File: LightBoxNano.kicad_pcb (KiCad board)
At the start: 2 copper layers, 63 parts, among them J5V1 Conn_02 DNP, SW1 Knitter-Switch DRR4010

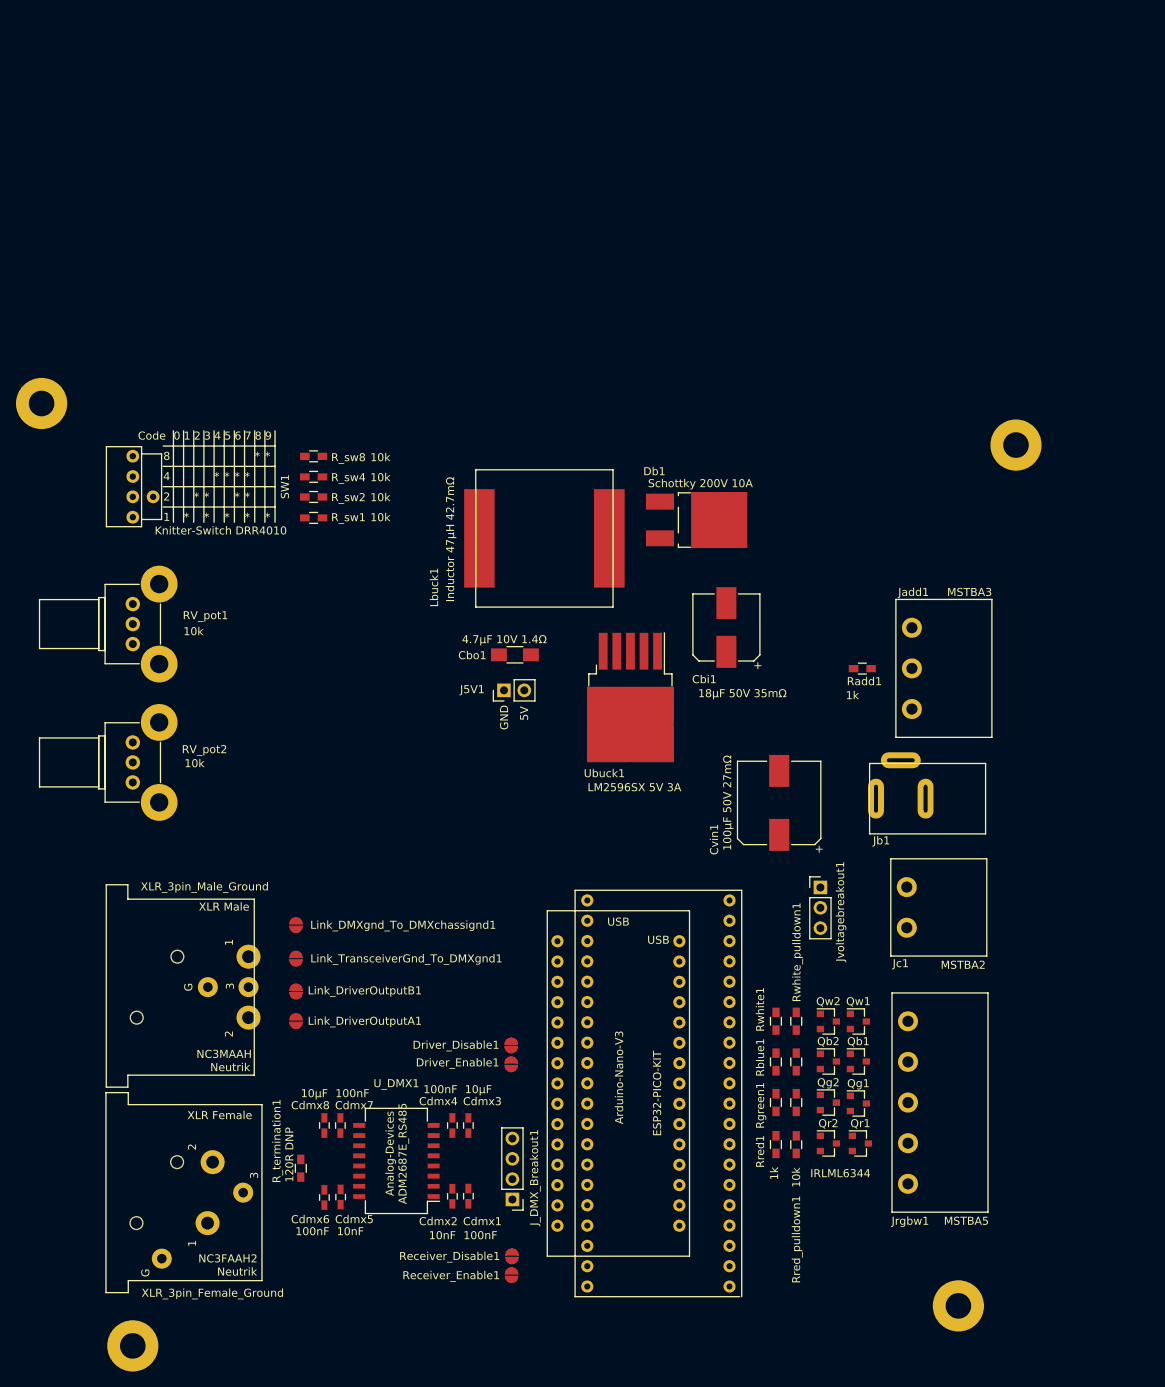
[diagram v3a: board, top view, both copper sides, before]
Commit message: Add Input Protection to PCB
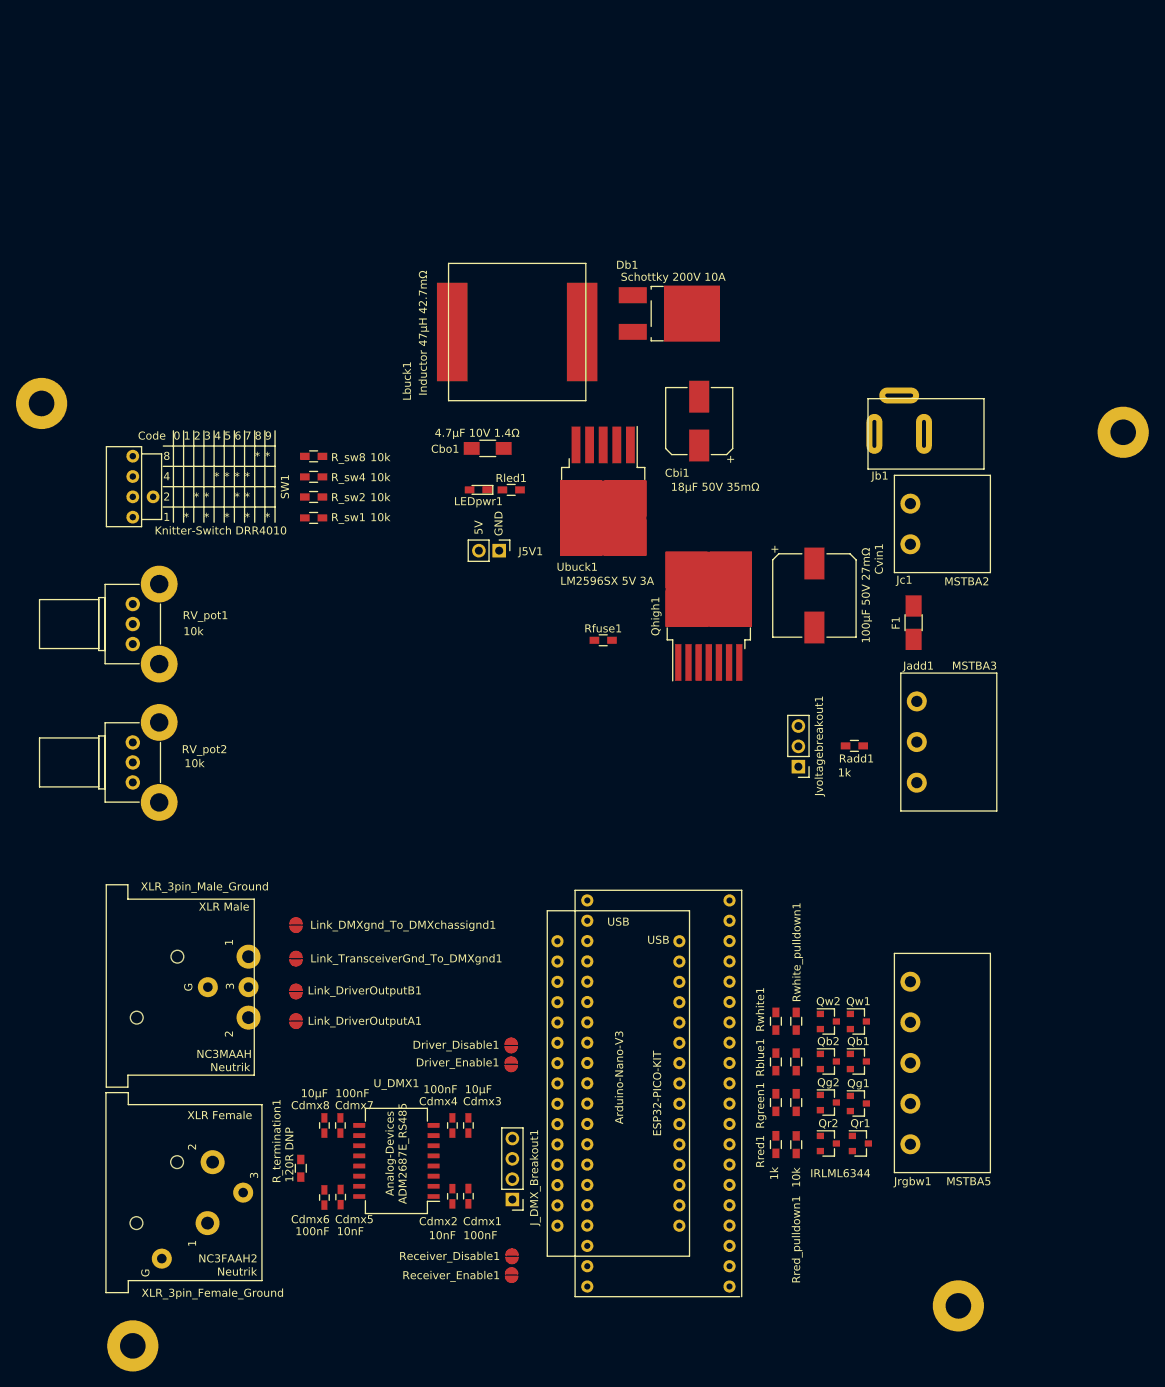
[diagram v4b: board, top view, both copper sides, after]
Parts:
- added F1: Fuse DNP, Fuse_Holders_and_Fuses:Fuse_SMD1206_HandSoldering, F.Cu at (195.0, 57.8)
- added LEDpwr1: LED Red, LEDs:LED_0603_HandSoldering, F.Cu at (140.6, 41.2)
- added Qhigh1: BTS50055-1TMC, TO_SOT_Packages_SMD:TO-263-7_TabPin4, F.Cu at (169.4, 57.0)
- added Rfuse1: 1k, Resistors_SMD:R_0603_HandSoldering, F.Cu at (156.2, 60.0)
- added Rled1: 300R, Resistors_SMD:R_0603_HandSoldering, F.Cu at (144.7, 41.2)
- moved Jc1 47.9 mm to (194.6, 48.0)
- moved Jb1 45.6 mm to (193.2, 34.2)
- moved Cvin1 26.3 mm to (182.6, 54.4), turned to 270 degrees
- moved Cbo1 26.0 mm to (141.8, 36.0)
- moved Ubuck1 26.0 mm to (156.2, 41.4)
- moved Cbi1 26.0 mm to (168.2, 32.6)
- moved Lbuck1 26.0 mm to (145.4, 21.5)
- moved Db1 26.0 mm to (164.5, 19.2)
- moved J5V1 17.5 mm to (143.2, 48.8), turned to 270 degrees
- moved Jvoltagebreakout1 15.3 mm to (180.6, 75.8), turned to 180 degrees
- moved H3 13.5 mm to (221.2, 34.0)
- moved Radd1 9.71 mm to (187.6, 73.2)
- moved Jadd1 9.23 mm to (195.4, 77.8)
- moved Jrgbw1 4.95 mm to (194.6, 123.0)
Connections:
- Cbi1 pad 1: /Vin -> /Vin_fused
- Jadd1 pad 1: /Vin -> GND
- Jadd1 pad 3: GND -> /Vin_fused
- Jrgbw1 pad 1: /Vin -> Net-(Jrgbw1-Pad1)
- Jrgbw1 pad 5: Net-(Jrgbw1-Pad5) -> /Vin_fused
- Jvoltagebreakout1 pad 3: /Vin -> /Vin_fused
- Qb1 pad 3: Net-(Jrgbw1-Pad4) -> Net-(Jrgbw1-Pad3)
- Qb2 pad 3: Net-(Jrgbw1-Pad4) -> Net-(Jrgbw1-Pad3)
- Qg1 pad 3: Net-(Jrgbw1-Pad3) -> Net-(Jrgbw1-Pad2)
- Qg2 pad 3: Net-(Jrgbw1-Pad3) -> Net-(Jrgbw1-Pad2)
- Qr1 pad 3: Net-(Jrgbw1-Pad2) -> Net-(Jrgbw1-Pad1)
- Qr2 pad 3: Net-(Jrgbw1-Pad2) -> Net-(Jrgbw1-Pad1)
- Qw1 pad 3: Net-(Jrgbw1-Pad5) -> Net-(Jrgbw1-Pad4)
- Qw2 pad 3: Net-(Jrgbw1-Pad5) -> Net-(Jrgbw1-Pad4)
- Radd1 pad 1: /Addressable -> Net-(Jadd1-Pad2)
- Radd1 pad 2: Net-(Jadd1-Pad2) -> /Addressable
- Ubuck1 pad 1: /Vin -> /Vin_fused

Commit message: Input Protection description, Pwer Switch Feedback
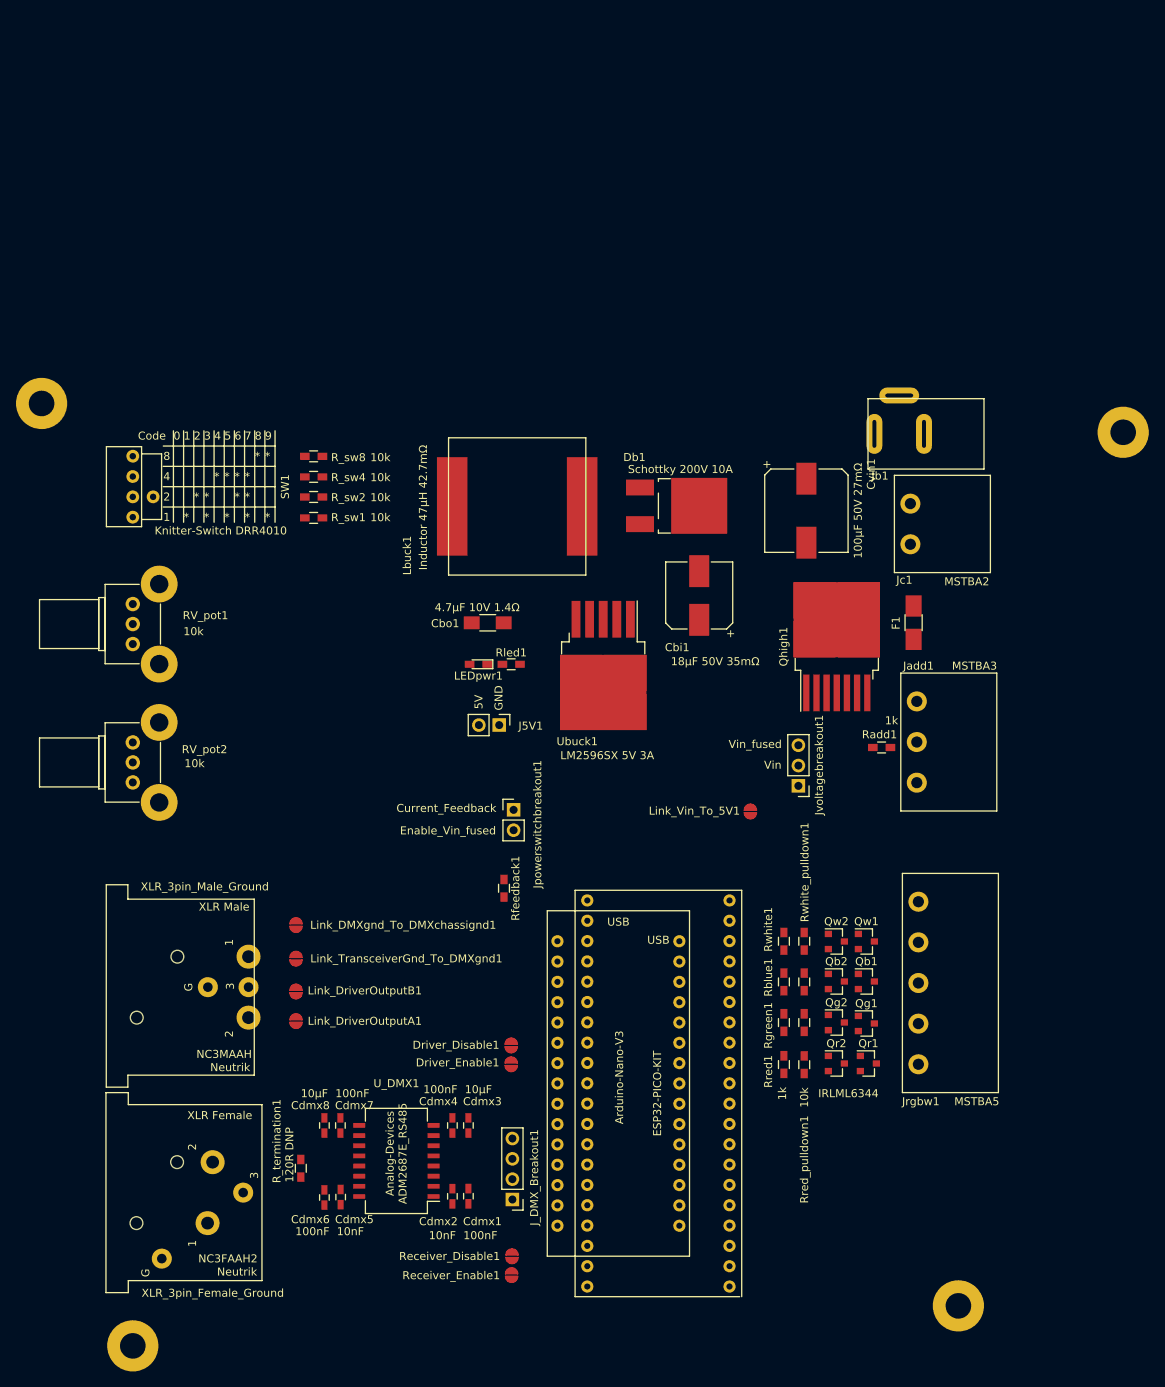
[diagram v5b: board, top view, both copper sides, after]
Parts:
- removed Rfuse1: 1k, Resistors_SMD:R_0603_HandSoldering
- added Jpowerswitchbreakout1: Conn_02 DNP, Pin_Headers:Pin_Header_Straight_1x02_Pitch2.54mm, F.Cu at (145.0, 81.2)
- added Link_Vin_To_5V1: Link Vin to 5V, ConnTest:JUMPER-SOLDER-SMD, F.Cu at (174.6, 81.4)
- added Rfeedback1: 1k, Resistors_SMD:R_0603_HandSoldering, F.Cu at (143.8, 91.0)
- moved Db1 24.0 mm to (165.4, 43.2)
- moved Cbo1 21.8 mm to (141.8, 57.8)
- moved Cbi1 21.8 mm to (168.2, 54.4)
- moved J5V1 21.8 mm to (143.2, 70.6)
- moved LEDpwr1 21.8 mm to (140.6, 63.0)
- moved Lbuck1 21.8 mm to (145.4, 43.3)
- moved Rled1 21.8 mm to (144.7, 63.0)
- moved Ubuck1 21.8 mm to (156.2, 63.1)
- moved Qhigh1 16.4 mm to (185.4, 60.8)
- moved Cvin1 10.6 mm to (181.6, 43.8)
- moved Jrgbw1 10.0 mm to (195.6, 113.0)
- moved Qb1 10.0 mm to (189.1, 102.7)
- moved Qb2 10.0 mm to (185.3, 102.7)
- moved Qg1 10.0 mm to (189.1, 107.9)
- moved Qg2 10.0 mm to (185.3, 107.8)
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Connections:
- Cbi1 pad 1: /Vin_fused -> /Vin
- MCU_esp1 pad J2_16: Net-(MCU_esp1-PadJ2_16) -> /Current_Feedback
- MCU_esp1 pad J2_17: Net-(MCU_esp1-PadJ2_17) -> /Enable_Vin_fused
- MCU_nano1 pad 16: Net-(MCU_nano1-Pad16) -> /Enable_Vin_fused
- MCU_nano1 pad 19: Net-(MCU_nano1-Pad19) -> /Current_Feedback
- Qhigh1 pad 3: GND -> /Enable_Vin_fused
- Qhigh1 pad 5: Net-(Qhigh1-Pad5) -> /Current_Feedback
- Ubuck1 pad 1: /Vin_fused -> /Vin

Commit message: Adjust PCB size to enclosure
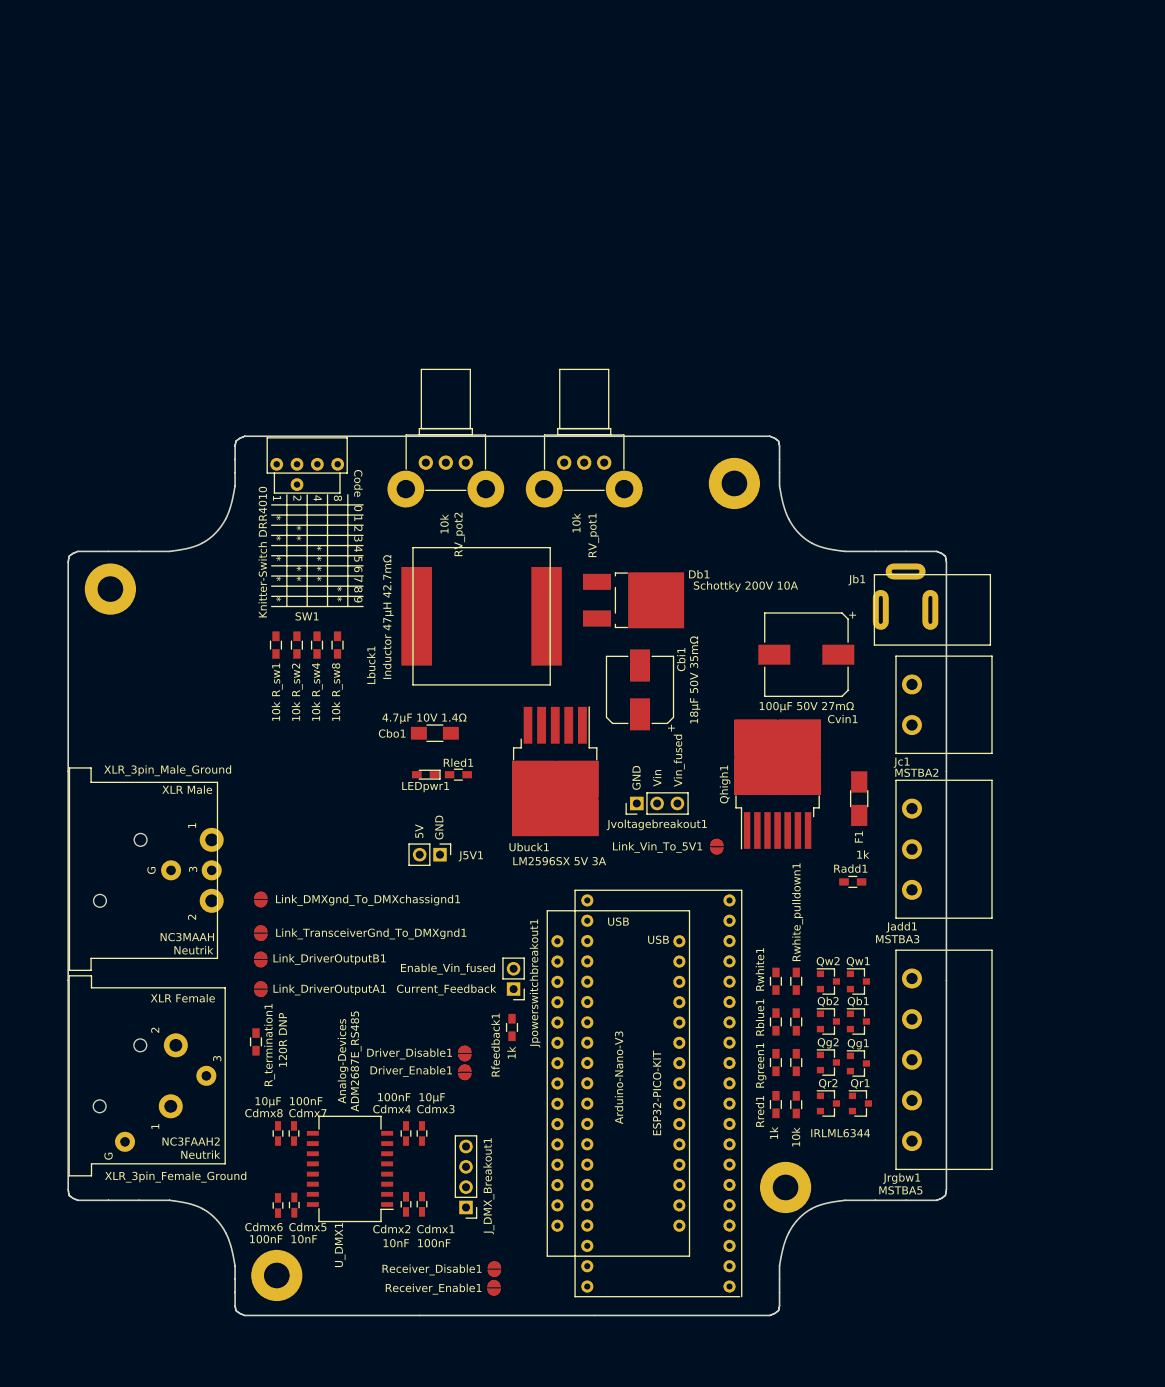
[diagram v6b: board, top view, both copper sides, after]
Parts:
- moved RV_pot1 61.5 mm to (156.3, 37.8), turned to 90 degrees
- moved RV_pot2 54.4 mm to (139.0, 37.8), turned to 90 degrees
- moved H3 49.0 mm to (172.6, 40.4)
- moved H4 26.2 mm to (179.0, 128.4)
- moved H1 24.7 mm to (94.6, 53.6)
- moved R_sw8 23.8 mm to (123.0, 60.6), turned to 90 degrees
- moved F1 23.0 mm to (188.2, 79.8)
- moved Jc1 22.6 mm to (194.8, 70.6)
- moved Jpowerswitchbreakout1 22.4 mm to (145.0, 103.6), turned to 180 degrees
- moved Jb1 22.0 mm to (194.0, 56.2)
- moved SW1 22.0 mm to (119.2, 38.0), turned to 0 degrees
- moved R_sw4 21.0 mm to (120.4, 60.6), turned to 90 degrees
- moved Jvoltagebreakout1 20.3 mm to (160.4, 80.4), turned to 90 degrees
- moved H2 20.0 mm to (115.4, 139.4)
- moved Qhigh1 18.7 mm to (178.0, 78.0)
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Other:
- board outline added: 109.8 x 109.9 mm
- copper layers 2 -> 4

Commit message: Start routing on PCB
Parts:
- moved Link_DMXgnd_To_DMXchassignd1 2.61 mm to (112.0, 90.2)
- moved Link_DriverOutputB1 2.61 mm to (112.0, 97.7)
- moved Link_DriverOutputA1 2.61 mm to (112.0, 101.4)
- moved Link_TransceiverGnd_To_DMXgnd1 2.61 mm to (112.0, 94.4)
- moved J5V1 2.55 mm to (137.6, 85.0)
- moved Link_Vin_To_5V1 2.15 mm to (171.2, 87.8)
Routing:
- net GND: track 0.00 -> 102.4 mm
- net /Vin: track 0.00 -> 98.1 mm
- net +5V: track 0.00 -> 93.7 mm, vias 0 -> 1
- net /DMX512/DMX+: track 0.00 -> 57.9 mm, vias 0 -> 1
- net /Vin_fused: track 0.00 -> 50.5 mm
- net /DMX512/DMXgnd: track 0.00 -> 36.4 mm
- net /DMX512/DMXchassignd: track 0.00 -> 36.3 mm
- net /SwCode2: track 0.00 -> 31.2 mm
- net /DMX512/DMX-: track 0.00 -> 30.6 mm
- net /SwCode1: track 0.00 -> 29.9 mm
- net /SwCode4: track 0.00 -> 29.9 mm
- net /SwCode8: track 0.00 -> 29.9 mm
- net /DMX_Receive: track 0.00 -> 28.1 mm
- net Net-(Db1-Pad1): track 0.00 -> 26.4 mm
- net /Gate_red: track 0.00 -> 21.5 mm
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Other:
- net class Fat added: clearance 0.2, trace_width 0.75, via_dia 0.8, via_drill 0.4

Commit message: Route PCB
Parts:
- moved Jvoltagebreakout1 3.16 mm to (161.4, 83.4)
- moved Link_Vin_To_5V1 1.97 mm to (172.0, 89.6)
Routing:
- net GND: track 102.4 -> 542.3 mm, vias 0 -> 10
- net +3V3: track 8.96 -> 208.6 mm, vias 0 -> 4
- net /POT_1: track 4.79 -> 101.5 mm
- net /SwCode1: track 29.9 -> 115.5 mm
- net /SwCode2: track 31.2 -> 115.5 mm
- net /POT_2: track 4.79 -> 83.3 mm
- net /SwCode4: track 29.9 -> 102.1 mm
- net /SwCode8: track 29.9 -> 98.8 mm
- net +5V: track 93.7 -> 141.3 mm, vias 1 -> 0
- net /DMX512/GND2: track 10.2 -> 57.7 mm, vias 0 -> 3
- net /Addressable: track 10.2 -> 56.4 mm, vias 0 -> 2
- net /Current_Feedback: track 14.7 -> 54.3 mm, vias 0 -> 2
- net /DMX512/DMX-: track 30.6 -> 65.5 mm, vias 0 -> 1
- net /Enable_Vin_fused: track 12.4 -> 46.6 mm, vias 0 -> 2
- net /DMX512/DMXTransmitterY: track 0.00 -> 31.2 mm, vias 0 -> 2
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- added copper zone on B.Cu, net GND
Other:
- copper layers 4 -> 2
